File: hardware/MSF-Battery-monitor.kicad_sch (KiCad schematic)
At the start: 34 parts, among them J1 Chargeur_in, J2 Chargeur_out, J3 USB_B_Mini, J5 PROG, J6 Load_in, J7 Load_out, Q1 BSS138, Q2 IRLML6402, Q3 BSS138, U1 LM358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

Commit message: seconde tentative
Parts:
- added C6, C7, C8, C9: 10u, Capacitor_THT:CP_Radial_D6.3mm_P2.50mm, symbol Device:CP
- added R15, R19: 1k, Resistor_THT:R_Axial_DIN0207_L6.3mm_D2.5mm_P10.16mm_Horizontal, symbol Device:R
- added R16: 15k, Resistor_THT:R_Axial_DIN0207_L6.3mm_D2.5mm_P10.16mm_Horizontal, symbol Device:R
- added R18: 5.1k, Resistor_THT:R_Axial_DIN0207_L6.3mm_D2.5mm_P10.16mm_Horizontal, symbol Device:R
- added R20, R21: 10k, Resistor_THT:R_Axial_DIN0207_L6.3mm_D2.5mm_P10.16mm_Horizontal, symbol Device:R
- added U5: MCP9700AT-ELT, Package_TO_SOT_SMD:SOT-353_SC-70-5, symbol Sensor_Temperature:MCP9700AT-ELT
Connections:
- net +5V: now also U5.4 (Vdd)
- net GND: now also C6.2, C7.2, C8.2, C9.2, R18.2, R21.2, U5.2 (GND)
- net at R10.1, U1.1: now also R19.2; no longer U2.3 (AN1/VREF-/CN3/RA1)
- net at R5.1, U1.7: now also R15.2; no longer U2.2 (AN0/VREF+/CN2/RA0)
- net at J1.4 (Pin_4), J2.4 (Pin_4): now also R16.1
- net temperature: now reaches U2.26 (AN9/DAC1LN/RP15/CN11/PMCS1/RB15)
- net temperature: now also U5.3 (Vout)
- net Chargeur_Vin: now reaches U2.6 (AN4/C1IN-/RP2/CN6/RB2)
- net Chargeur_Vin: now also C7.1, R16.2, R18.1
- net Load_Vin: now reaches U2.7 (AN5/C1IN+/RP3/CN7/RB3)
- net Load_Vin: now also C9.1, R20.2, R21.1
- net at J6.4 (Pin_4), J7.4 (Pin_4): now also R20.1
- new net: C6.1, R15.1, U2.2 (AN0/VREF+/CN2/RA0)
- new net: C8.1, R19.1, U2.3 (AN1/VREF-/CN3/RA1)
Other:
- moved on the sheet: C3, C4, C5, J3, J6, J7, R10, R12, R6, R7, R8, R9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

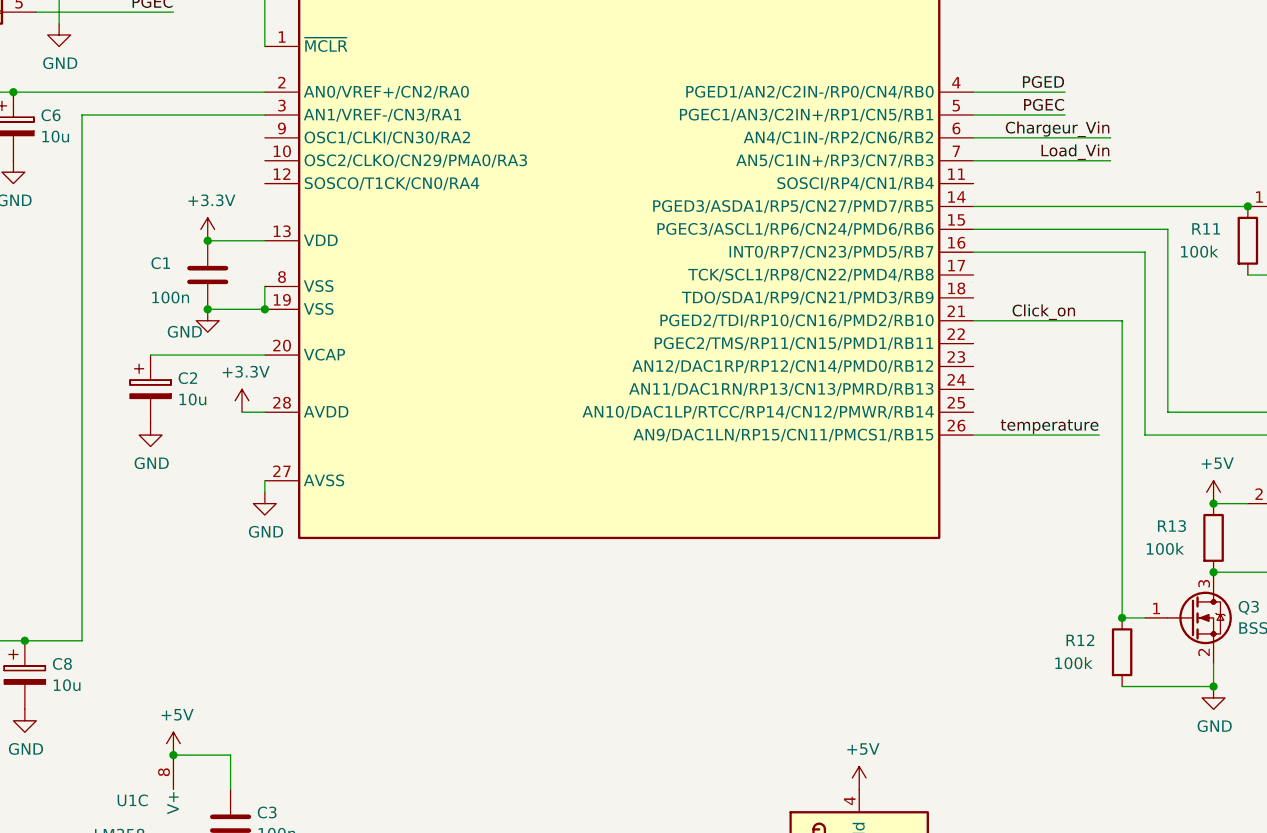
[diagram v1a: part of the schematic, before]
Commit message: passage au timer1 et mise à jour du PCB
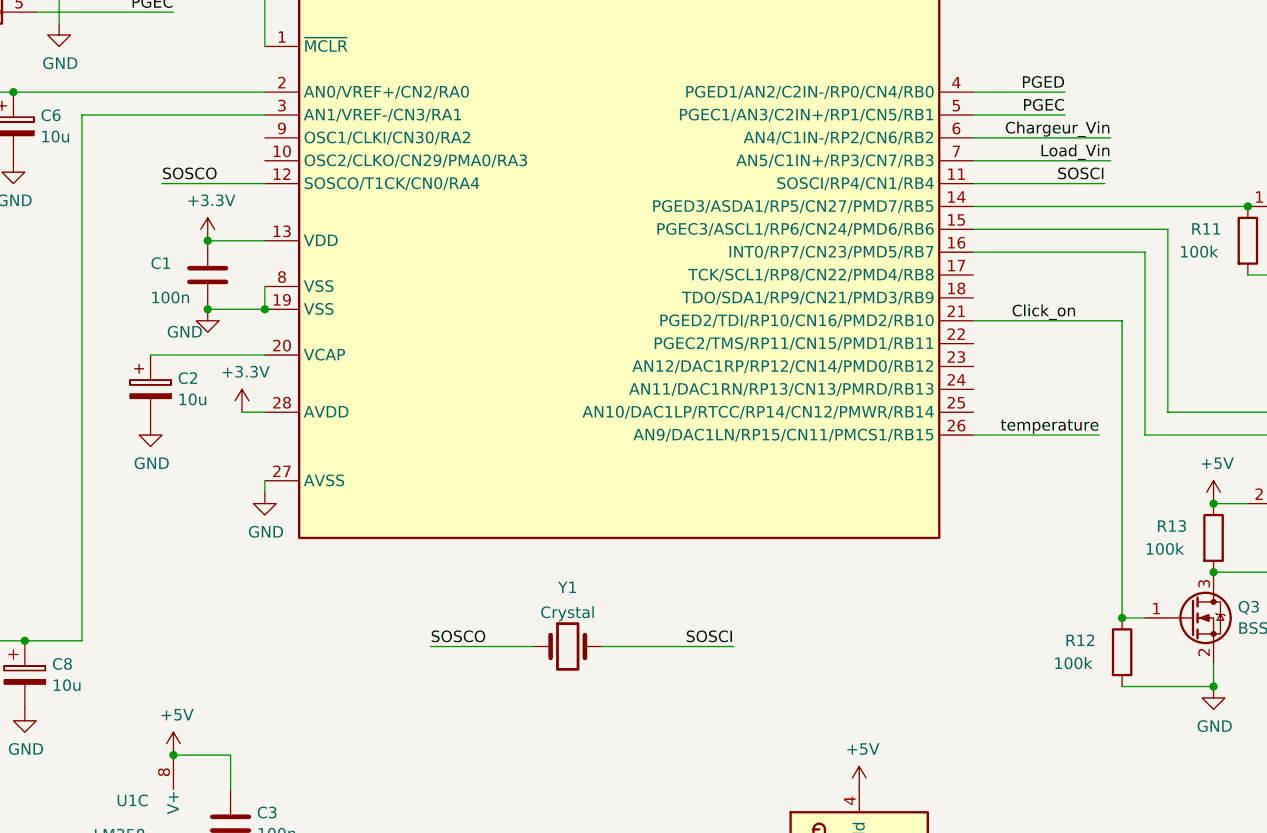
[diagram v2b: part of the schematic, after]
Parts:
- added Y1: Crystal, Crystal:Crystal_AT310_D3.0mm_L10.0mm_Vertical, symbol Device:Crystal
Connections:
- net SOSCI: now reaches U2.11 (SOSCI/RP4/CN1/RB4)
- net SOSCI: now also Y1.2
- net SOSCO: now reaches U2.12 (SOSCO/T1CK/CN0/RA4)
- net SOSCO: now also Y1.1
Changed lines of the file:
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@@
+    (stroke (width 0) (type default) (color 0 0 0 0))
+  )
+  (wire (pts (xy 133.985 123.825) (xy 145.415 123.825))
     (stroke (width 0) (type default) (color 0 0 0 0))
   )
@@
     (stroke (width 0) (type default) (color 0 0 0 0))
   )
+  (wire (pts (xy 194.31 72.39) (xy 208.915 72.39))
+    (stroke (width 0) (type default) (color 0 0 0 0))
+  )
   (wire (pts (xy 26.67 130.81) (xy 31.75 130.81))
     (stroke (width 0) (type default) (color 0 0 0 0))
@@
     (stroke (width 0) (type default) (color 0 0 0 0))
   )
+  (wire (pts (xy 104.14 72.39) (xy 115.57 72.39))
+    (stroke (width 0) (type default) (color 0 0 0 0))
+  )
   (wire (pts (xy 40.64 81.28) (xy 26.67 81.28))
     (stroke (width 0) (type default) (color 0 0 0 0))
@@
   )
   (wire (pts (xy 40.64 137.16) (xy 40.64 138.43))
+    (stroke (width 0) (type default) (color 0 0 0 0))
+  )
+  (wire (pts (xy 153.035 123.825) (xy 167.64 123.825))
     (stroke (width 0) (type default) (color 0 0 0 0))
   )
@@
     (effects (font (size 1.27 1.27)) (justify right bottom))
   )
+  (label "SOSCI" (at 208.915 72.39 180)
+    (effects (font (size 1.27 1.27)) (justify right bottom))
+  )
   (label "temperature" (at 209.55 147.32 180)
     (effects (font (size 1.27 1.27)) (justify right bottom))
@@
     (effects (font (size 1.27 1.27)) (justify right bottom))
   )
+  (label "SOSCO" (at 133.985 123.825 0)
+    (effects (font (size 1.27 1.27)) (justify left bottom))
+  )
   (label "Chargeur_Vin" (at 209.55 67.31 180)
     (effects (font (size 1.27 1.27)) (justify right bottom))
   )
+  (label "SOSCO" (at 104.14 72.39 0)
+    (effects (font (size 1.27 1.27)) (justify left bottom))
+  )
   (label "PGED" (at 105.41 50.8 180)
     (effects (font (size 1.27 1.27)) (justify right bottom))
@@
   )
   (label "PGEC" (at 105.41 53.34 180)
+    (effects (font (size 1.27 1.27)) (justify right bottom))
+  )
+  (label "SOSCI" (at 167.64 123.825 180)
     (effects (font (size 1.27 1.27)) (justify right bottom))
   )
@@
     (pin "1")
   )
+  (symbol (lib_id "Device:Crystal") (at 149.225 123.825 0) (unit 1)
+    (in_bom yes) (on_board yes) (fields_autoplaced)
+    (property "Reference" "Y1" (id 0) (at 149.225 117.2931 0))
+    (property "Value" "Crystal" (id 1) (at 149.225 120.0682 0))
+    (property "Footprint" "Crystal:Crystal_AT310_D3.0mm_L10.0mm_Vertical" (id 2) (at 149.225 123.825 0)
+      (effects (font (size 1.27 1.27)) hide)
+    )
+    (property "Datasheet" "~" (id 3) (at 149.225 123.825 0)
+      (effects (font (size 1.27 1.27)) hide)
+    )
+    (pin "1")
+    (pin "2")
+  )
   (symbol (lib_id "Connector:USB_B_Mini") (at 92.71 177.8 0) (unit 1)
     (in_bom yes) (on_board yes) (fields_autoplaced)
@@
       (reference "U5") (unit 1) (value "MCP9700AT-ELT") (footprint "Package_TO_SOT_SMD:SOT-353_SC-70-5")
     )
-  )
+    (path "/13ca6f98-495b-4848-a1b9-619bdbf2e008"
+      (reference "Y1") (unit 1) (value "Crystal") (footprint "Crystal:Crystal_AT310_D3.0mm_L10.0mm_Vertical")
+    )
+  )
